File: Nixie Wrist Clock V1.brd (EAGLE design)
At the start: 160 x 100 mm, 35 parts, among them Q1 310mA/60V/1.6Ω, Q2 310mA/60V/1.6Ω, Q3 310mA/60V/1.6Ω, Q4 310mA/60V/1.6Ω, Q5 310mA/60V/1.6Ω, U2 NRF52832, X3 32MHz, X4 32.768kHz

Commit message: Update (Alp)
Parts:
- moved X3 29.8 mm to (57.4, 47.4)
- moved C1 29.8 mm to (58.7, 25.9)
- moved C14 29.8 mm to (59.7, 47.6)
- moved C15 29.8 mm to (56.6, 38.0)
- moved C16 29.8 mm to (46.4, 41.1)
- moved C18 29.8 mm to (58.1, 42.0)
- moved C20 29.8 mm to (53.3, 44.8)
- moved X4 29.8 mm to (43.3, 42.1)
- moved C13 29.8 mm to (55.2, 47.5)
- moved C17 29.8 mm to (45.4, 34.2)
- moved C19 29.8 mm to (56.6, 42.0)
- moved C21 29.8 mm to (46.4, 44.7)
- moved C23 29.8 mm to (41.3, 44.2)
- moved L2 29.8 mm to (58.2, 37.5)
- moved U2 29.8 mm to (51.4, 38.0)
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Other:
- board size 160 x 100 mm -> 88.1 x 64.2 mm

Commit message: Update
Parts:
- added U$3: TLV70233SOT23-5, Alp-Special:SOT23-5
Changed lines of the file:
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@@
 <attribute name="VALUE" x="16.4846" y="22.5044" size="0.4064" layer="27" font="vector"/>
+</element>
+<element name="U$3" library="Alp-Special" package="SOT23-5" value="TLV70233SOT23-5" x="3.048" y="-2.032" smashed="yes">
+<attribute name="NAME" x="1.143" y="-2.032" size="0.6096" layer="25" font="vector" ratio="20" rot="R90" align="bottom-center"/>
+<attribute name="VALUE" x="5.588" y="-2.032" size="0.6096" layer="27" font="vector" ratio="20" rot="R90" align="bottom-center"/>
 </element>
 </elements>

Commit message: alp update
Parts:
- moved U$3 52.2 mm to (18.8, 47.8), turned to 90 degrees
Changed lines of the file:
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@@
 <attribute name="VALUE" x="16.4846" y="22.5044" size="0.4064" layer="27" font="vector"/>
 </element>
-<element name="U$3" library="Alp-Special" package="SOT23-5" value="TLV70233SOT23-5" x="3.048" y="-2.032" smashed="yes">
-<attribute name="NAME" x="1.143" y="-2.032" size="0.6096" layer="25" font="vector" ratio="20" rot="R90" align="bottom-center"/>
-<attribute name="VALUE" x="5.588" y="-2.032" size="0.6096" layer="27" font="vector" ratio="20" rot="R90" align="bottom-center"/>
+<element name="U$3" library="Alp-Special" package="SOT23-5" value="TLV70233SOT23-5" x="18.796" y="47.752" smashed="yes" rot="R90">
+<attribute name="NAME" x="18.796" y="45.847" size="0.6096" layer="25" font="vector" ratio="20" rot="R180" align="bottom-center"/>
+<attribute name="VALUE" x="18.796" y="50.292" size="0.6096" layer="27" font="vector" ratio="20" rot="R180" align="bottom-center"/>
 </element>
 </elements>

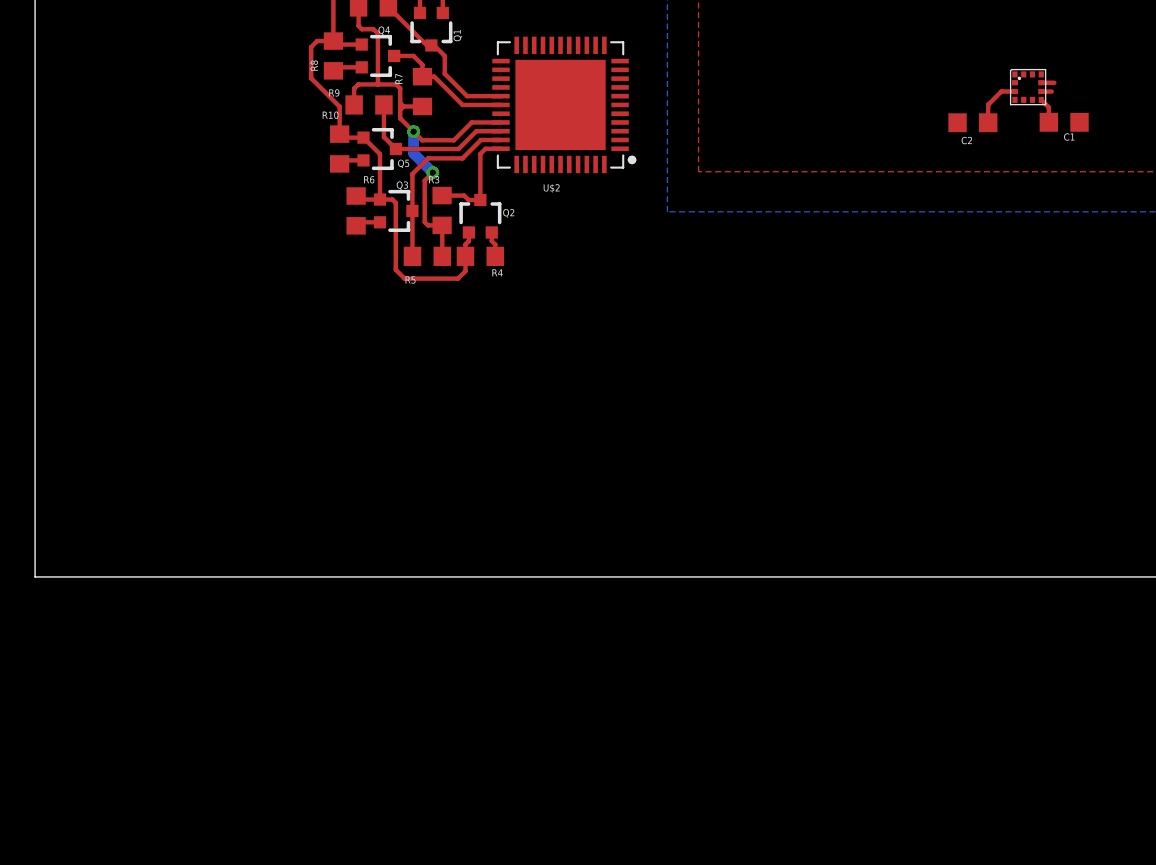
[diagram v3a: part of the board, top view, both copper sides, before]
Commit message: 3v3 LDO added
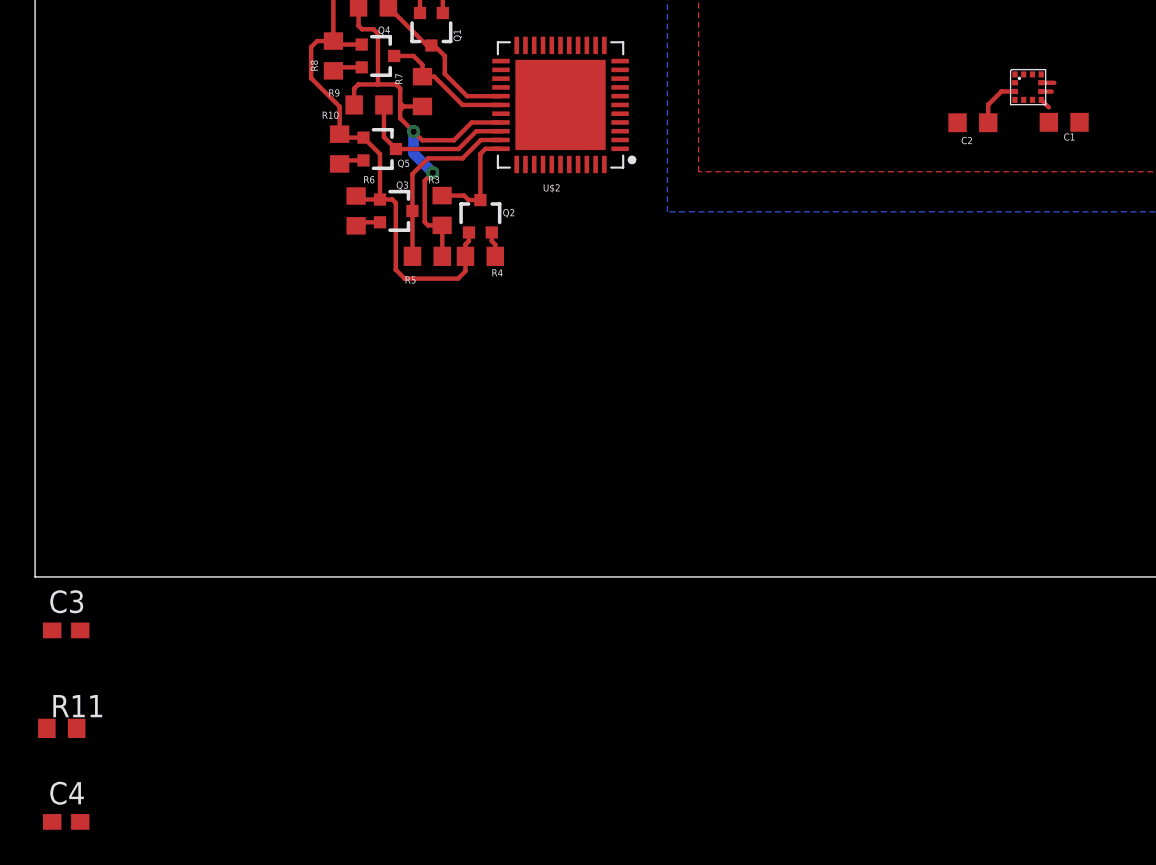
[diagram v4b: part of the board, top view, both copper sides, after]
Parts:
- added C3, C4: 100nF, Nordic_nRF:RESC0603_N
- added R11: 10K, rcl:R0603
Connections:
- new net 3V3-ENABLE: U$3.3
- new net VCC: C4.1, U$3.1
- net +3V3: now also C3.1, U$3.5
- net GND: now also C3.2, C4.2, U$3.2, U$3.4
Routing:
- net +3V3: track 72.9 -> 72.0 mm
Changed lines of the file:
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@@
 <attribute name="VALUE" x="18.796" y="50.292" size="0.6096" layer="27" font="vector" ratio="20" rot="R180" align="bottom-center"/>
+</element>
+<element name="C3" library="Nordic_nRF" package="RESC0603_N" value="100nF" x="1.778" y="-3.048" smashed="yes">
+<attribute name="NAME" x="0.778" y="-2.048" size="1.27" layer="25"/>
+<attribute name="VALUE" x="0.778" y="-5.548" size="1.27" layer="27"/>
+</element>
+<element name="R11" library="rcl" library_urn="urn:adsk.eagle:library:334" package="R0603" package3d_urn="urn:adsk.eagle:package:23555/3" value="10K" x="1.524" y="-8.636" smashed="yes">
+<attribute name="NAME" x="0.889" y="-8.001" size="1.27" layer="25"/>
+<attribute name="SPICEPREFIX" value="R" x="1.524" y="-8.636" size="1.778" layer="27" display="off"/>
+<attribute name="VALUE" x="0.889" y="-10.541" size="1.27" layer="27"/>
+</element>
+<element name="C4" library="Nordic_nRF" package="RESC0603_N" value="100nF" x="1.778" y="-13.97" smashed="yes">
+<attribute name="NAME" x="0.778" y="-12.97" size="1.27" layer="25"/>
+<attribute name="VALUE" x="0.778" y="-16.47" size="1.27" layer="27"/>
 </element>
 </elements>
@@
 <wire x1="57.396" y1="27.686" x2="57.9882" y2="27.686" width="0.254" layer="1"/>
 <wire x1="57.392" y1="28.19" x2="58.1366" y2="28.19" width="0.254" layer="1"/>
+<contactref element="C4" pad="2"/>
+<contactref element="U$3" pad="2"/>
+<contactref element="U$3" pad="4"/>
+<contactref element="C3" pad="2"/>
+<wire x1="58.003" y1="48.0854" x2="59.686" y2="48.401" width="0" layer="19" extent="1-1"/>
+<wire x1="56.853" y1="46.6354" x2="58.003" y2="48.0854" width="0" layer="19" extent="1-1"/>
+<wire x1="56.0578" y1="45.3136" x2="56.853" y2="46.6354" width="0" layer="19" extent="1-1"/>
+<wire x1="55.186" y1="48.322" x2="56.853" y2="46.6354" width="0" layer="19" extent="1-1"/>
+<wire x1="56.5876" y1="42.8222" x2="56.0578" y2="45.3136" width="0" layer="19" extent="1-1"/>
+<wire x1="58.1464" y1="42.8222" x2="56.5876" y2="42.8222" width="0" layer="19" extent="1-1"/>
+<wire x1="53.297" y1="45.6042" x2="56.0578" y2="45.3136" width="0" layer="19" extent="1-1"/>
+<wire x1="49.6876" y1="45.5772" x2="53.297" y2="45.6042" width="0" layer="19" extent="1-1"/>
+<wire x1="46.4284" y1="45.4794" x2="49.6876" y2="45.5772" width="0" layer="19" extent="1-1"/>
+<wire x1="46.4238" y1="41.898" x2="46.4284" y2="45.4794" width="0" layer="19" extent="1-1"/>
+<wire x1="49.586" y1="39.804" x2="46.4238" y2="41.898" width="0" layer="19" extent="1-1"/>
+<wire x1="41.34" y1="44.966" x2="46.4284" y2="45.4794" width="0" layer="19" extent="1-1"/>
+<wire x1="44.588" y1="34.158" x2="49.586" y2="36.204" width="0" layer="19" extent="1-1"/>
+<wire x1="41.337" y1="39.2458" x2="41.34" y2="44.966" width="0" layer="19" extent="1-1"/>
+<wire x1="57.392" y1="28.19" x2="53.186" y2="36.204" width="0" layer="19" extent="1-1"/>
+<wire x1="57.392" y1="27.69" x2="57.392" y2="28.19" width="0" layer="19" extent="1-1"/>
+<wire x1="59.5744" y1="25.9334" x2="57.9882" y2="27.686" width="0" layer="19" extent="1-1"/>
+<wire x1="52.6174" y1="25.908" x2="57.392" y2="27.69" width="0" layer="19" extent="1-1"/>
+<wire x1="29.972" y1="26.924" x2="44.588" y2="34.158" width="0" layer="19" extent="1-1"/>
 <wire x1="26.5762" y1="26.424" x2="29.972" y2="26.924" width="0" layer="19" extent="1-1"/>
-<wire x1="41.337" y1="39.2458" x2="29.972" y2="26.924" width="0" layer="19" extent="1-1"/>
+<wire x1="20.0961" y1="47.752" x2="41.34" y2="44.966" width="0" layer="19" extent="1-1"/>
+<wire x1="17.4959" y1="48.702" x2="20.0961" y2="47.752" width="0" layer="19" extent="1-1"/>
+<wire x1="2.578" y1="-3.048" x2="26.5762" y2="26.424" width="0" layer="19" extent="1-1"/>
+<wire x1="2.578" y1="-13.97" x2="2.578" y2="-3.048" width="0" layer="19" extent="1-1"/>
 </signal>
 <signal name="DEC1">
@@
 <contactref element="U2" pad="13"/>
 <contactref element="C17" pad="1"/>
-<contactref element="U$1" pad="3"/>
-<contactref element="C2" pad="1"/>
-<contactref element="U$1" pad="7"/>
-<contactref element="C1" pad="2"/>
 <contactref element="U2" pad="36"/>
 <contactref element="C20" pad="1"/>
@@
 <contactref element="Q5" pad="1"/>
 <contactref element="R10" pad="2"/>
-<wire x1="57.392" y1="27.215" x2="57.8244" y2="26.7826" width="0.254" layer="1"/>
-<wire x1="57.8244" y1="26.7826" x2="57.8244" y2="25.9334" width="0.254" layer="1"/>
-<wire x1="55.892" y1="27.69" x2="55.121421875" y2="27.69" width="0.254" layer="1"/>
-<wire x1="55.121421875" y1="27.69" x2="54.3651" y2="26.93265" width="0.254" layer="1"/>
-<wire x1="54.3651" y1="26.93265" x2="54.3674" y2="25.908" width="0.254" layer="1"/>
-<wire x1="54.3674" y1="25.908" x2="54.3928" y2="25.9334" width="0.254" layer="1"/>
 <wire x1="24.75" y1="19.649" x2="24.75" y2="19.162" width="0.254" layer="1"/>
 <wire x1="24.55" y1="18.962" x2="24.55" y2="18.288" width="0.254" layer="1"/>
@@
 <wire x1="20.574" y1="33.782" x2="17.78" y2="33.782" width="0.254" layer="1"/>
 <wire x1="17.78" y1="33.782" x2="17.018" y2="33.02" width="0.254" layer="1"/>
+<contactref element="U$1" pad="3"/>
+<contactref element="C2" pad="1"/>
+<contactref element="C1" pad="2"/>
+<contactref element="U$1" pad="7"/>
+<wire x1="55.892" y1="27.69" x2="55.121421875" y2="27.69" width="0.254" layer="1"/>
+<wire x1="55.121421875" y1="27.69" x2="54.3651" y2="26.93265" width="0.254" layer="1"/>
+<wire x1="54.3651" y1="26.93265" x2="54.3674" y2="25.908" width="0.254" layer="1"/>
+<wire x1="54.3674" y1="25.908" x2="54.3928" y2="25.9334" width="0.254" layer="1"/>
+<wire x1="57.392" y1="27.215" x2="57.8244" y2="26.7826" width="0.254" layer="1"/>
+<contactref element="U$3" pad="5"/>
+<contactref element="C3" pad="1"/>
+<wire x1="57.8244" y1="26.7826" x2="57.8244" y2="25.9334" width="0" layer="19" extent="1-1"/>
 <wire x1="55.892" y1="27.69" x2="57.392" y2="27.215" width="0" layer="19" extent="1-1"/>
 <wire x1="49.186" y1="34.3524" x2="55.121421875" y2="27.69" width="0" layer="19" extent="1-1"/>
-<wire x1="23.456" y1="33.782" x2="46.188" y2="34.158" width="0" layer="19" extent="1-1"/>
+<wire x1="23.456" y1="33.782" x2="46.204" y2="34.174" width="0" layer="19" extent="1-1"/>
+<wire x1="17.4959" y1="46.802" x2="21.082" y2="35.052" width="0" layer="19" extent="1-1"/>
+<wire x1="0.978" y1="-3.048" x2="20.574" y2="17.526" width="0" layer="19" extent="1-1"/>
 </signal>
 <signal name="INT1">
@@
 <wire x1="17.5736" y1="23.7594" x2="17.3736" y2="23.5594" width="0.254" layer="1"/>
 </signal>
+<signal name="3V3-ENABLE">
+<contactref element="U$3" pad="3"/>
+</signal>
+<signal name="VCC">
+<contactref element="U$3" pad="1"/>
+<contactref element="C4" pad="1"/>
+<wire x1="0.978" y1="-13.97" x2="20.0961" y2="46.802" width="0" layer="19" extent="1-1"/>
+</signal>
 </signals>

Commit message: Update#7
5V Boost Regulator Added
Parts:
- added C10: 10uF, rcl:SMC_A
- added C11: 22uF, rcl:SMC_B
- added C5, C6, C7: 100nF, Nordic_nRF:RESC0603_N
- added C9: 100pF, Nordic_nRF:RESC0603_N
- added R12: 6.65K, rcl:R0603
- added R13: 768K, rcl:R0603
- added R14: 243K, rcl:R0603
- added R15: 868K, rcl:R0603
- added U$4: TPS61252DSGR, Alp-Special:WSON-8-PAD
- added U$5: FPI-SERIES-INDUCTOR0302, Alp-Special:FPI-0302
- moved C4 41.1 mm to (-30.7, -39.1)
- moved C3 2.05 mm to (1.52, -5.08)
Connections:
- new net 5V-ENA: U$4.6
- new net N$10: R15.2, U$4.5
- new net N$14: C9.2, R13.2, R14.1, U$4.3
- new net N$6: U$4.7, U$5.P$2
- new net N$8: R12.1, U$4.4
- net +5V: now also C11.+, C9.1, R13.1, R15.1, U$4.2
- net GND: now also C10.-, C11.-, R12.2, R14.2, U$4.1, U$4.PAD
- net VCC: now also C10.+, U$4.8, U$5.P$1

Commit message: Update#7
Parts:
- removed C5, C6, C7: 100nF, Nordic_nRF:RESC0603_N
- removed R11: 10K, rcl:R0603
- moved R14 17.1 mm to (-26.0, -34.3)
- moved C9 14.8 mm to (-29.3, -33.2)
- moved R15 14.7 mm to (-26.2, -28.9), turned to 180 degrees
- moved R12 14.5 mm to (-26.0, -32.1)
- moved C11 13.7 mm to (-32.8, -33.5), turned to 270 degrees
- moved R13 11.5 mm to (-29.3, -35.0)
- moved C4 9.88 mm to (-33.0, -29.5), turned to 180 degrees
- moved C10 7.76 mm to (-34.7, -27.6), turned to 180 degrees
- moved U$5 3.28 mm to (-30.1, -26.7), turned to 270 degrees
- moved U$4 2.96 mm to (-29.2, -30.5)
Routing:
- net N$6: track 0.00 -> 3.40 mm
- net N$8: track 0.00 -> 2.15 mm
- net N$14: track 0.00 -> 2.06 mm
- net +5V: track 27.7 -> 29.7 mm
- net N$10: track 0.00 -> 1.92 mm
- net GND: vias 1 -> 2
- added copper zone on layer 1, net N$14

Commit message: Update#7
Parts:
- added C5: 1pF, Nordic_nRF:RESC0402_N
- C15: value 0.8pF -> 1pF
- moved U$5 87.9 mm to (47.6, 14.3)
- moved C11 87.8 mm to (44.9, 7.37)
- moved C4 87.8 mm to (44.8, 11.4)
- moved C9 87.8 mm to (48.4, 7.67)
- moved R12 87.8 mm to (51.7, 8.84)
- moved R13 87.8 mm to (48.4, 5.89)
- moved R14 87.8 mm to (51.7, 6.55)
- moved U$4 87.8 mm to (48.5, 10.4)
- moved C10 87.8 mm to (43.0, 13.3)
- moved R15 87.8 mm to (51.6, 12.0)
- moved C3 25.0 mm to (14.2, 16.5)
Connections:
- net GND: now also C5.2
- net RF: now also C5.1
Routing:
- added copper zone on layer 1, net VCC
